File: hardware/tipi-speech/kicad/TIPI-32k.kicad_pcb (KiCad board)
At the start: 2 copper layers, 115.7 x 56 mm, 33 parts, among them J1 TI-99_Sideport, J2 USB_B_Micro, J3 Conn_01x02, P1 TI-99_Sideport, Q1 NPN_BCE, U1 XC95144XL-TQ100, U2 27C256, U3 74HCT245, U4 LM1117-3.3, U5 CY62256L-70PC

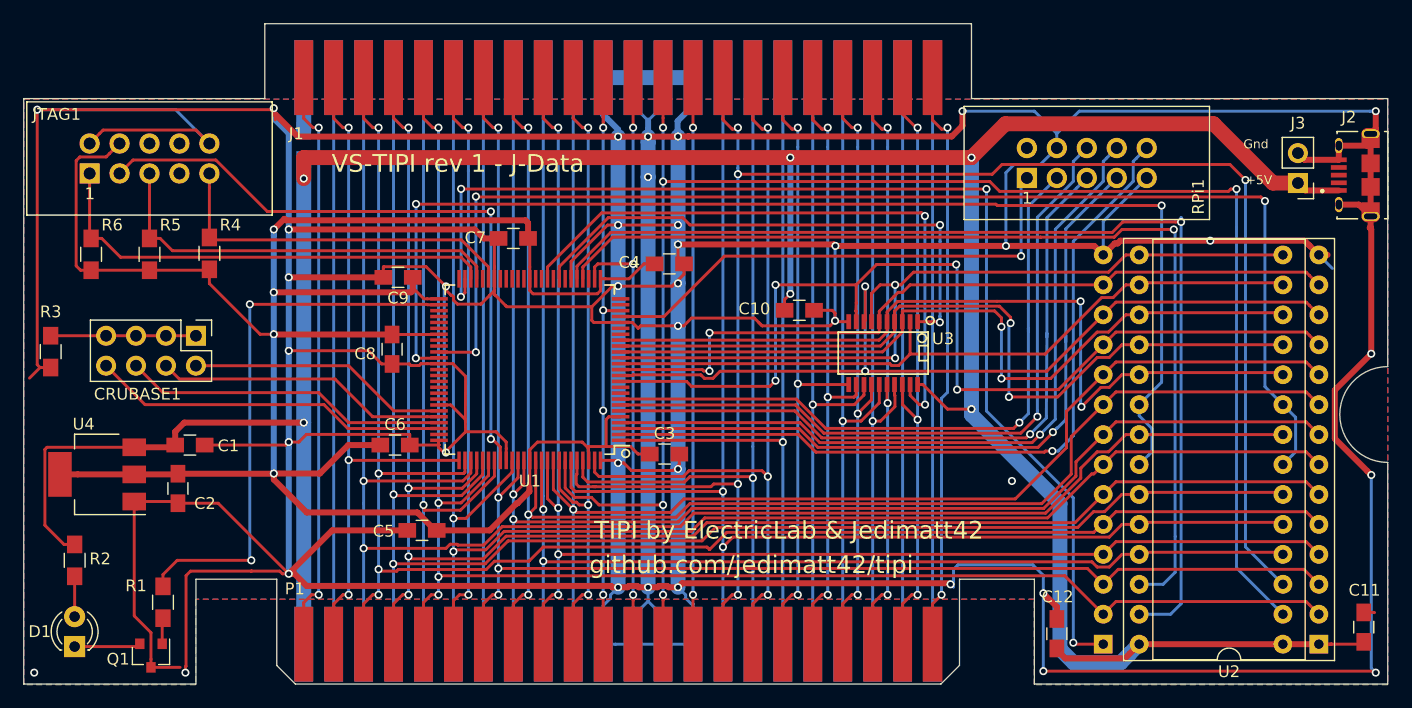
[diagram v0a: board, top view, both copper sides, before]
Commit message: TIPI/32K V2 PCB and V3 CPLD updates
This update is PCB manufacturability improvements (Via to trace increase and R7 moved to topside) and V3 CPLD changes to support RAM disable without CRU Address changes.
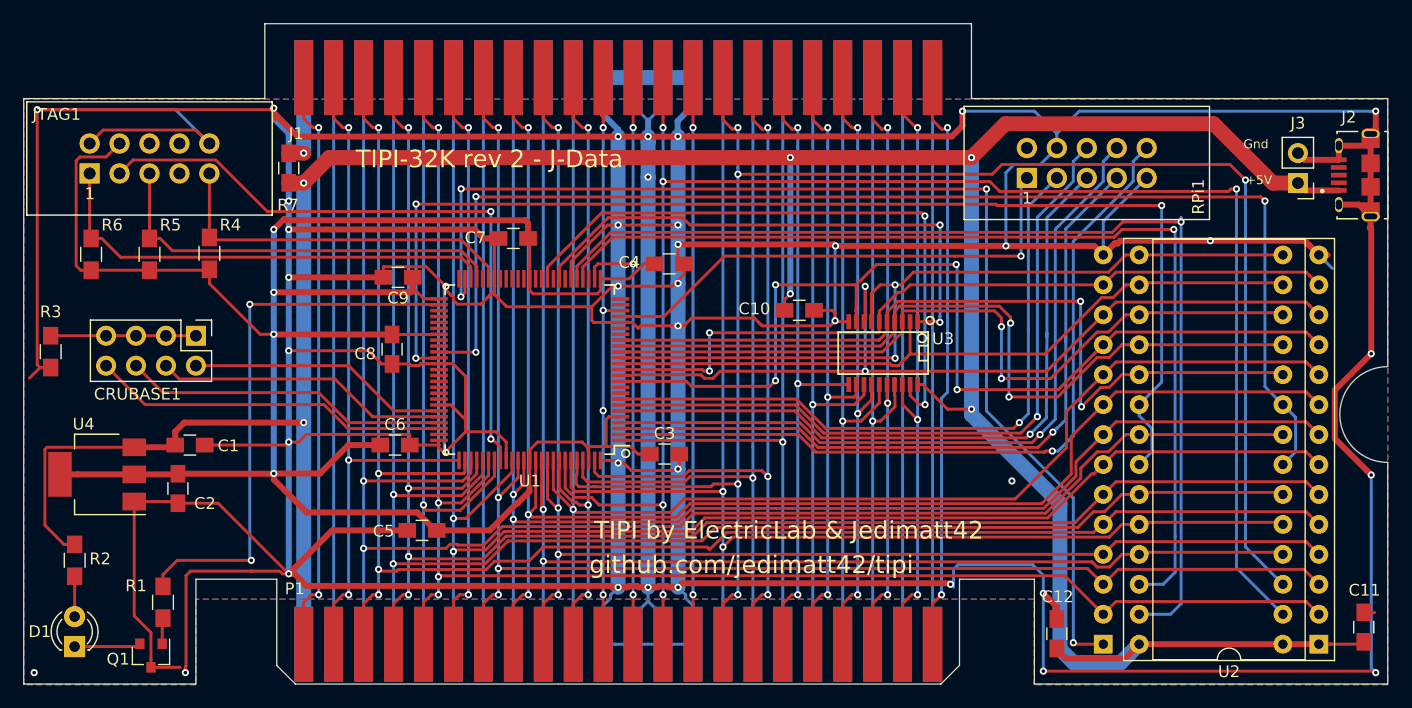
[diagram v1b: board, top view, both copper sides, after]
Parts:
- R7: moved to F.Cu
- moved R7 2.31 mm to (83.3, 101.4)
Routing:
- net Net-(J1-Pad1): track 6.48 -> 9.67 mm, vias 0 -> 1
- net +5V: track 271.7 -> 269.9 mm
- net GND: vias 39 -> 40
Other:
- rule via_min_drill: 0.3302 -> 0.3048
- rule via_min_size: 0.6858 -> 0.6096
- board text added: "TIPI-32K rev 2 - J-Data"
- board text removed: "VS-TIPI rev 1 - J-Data"
